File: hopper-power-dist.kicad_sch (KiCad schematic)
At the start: 23 parts

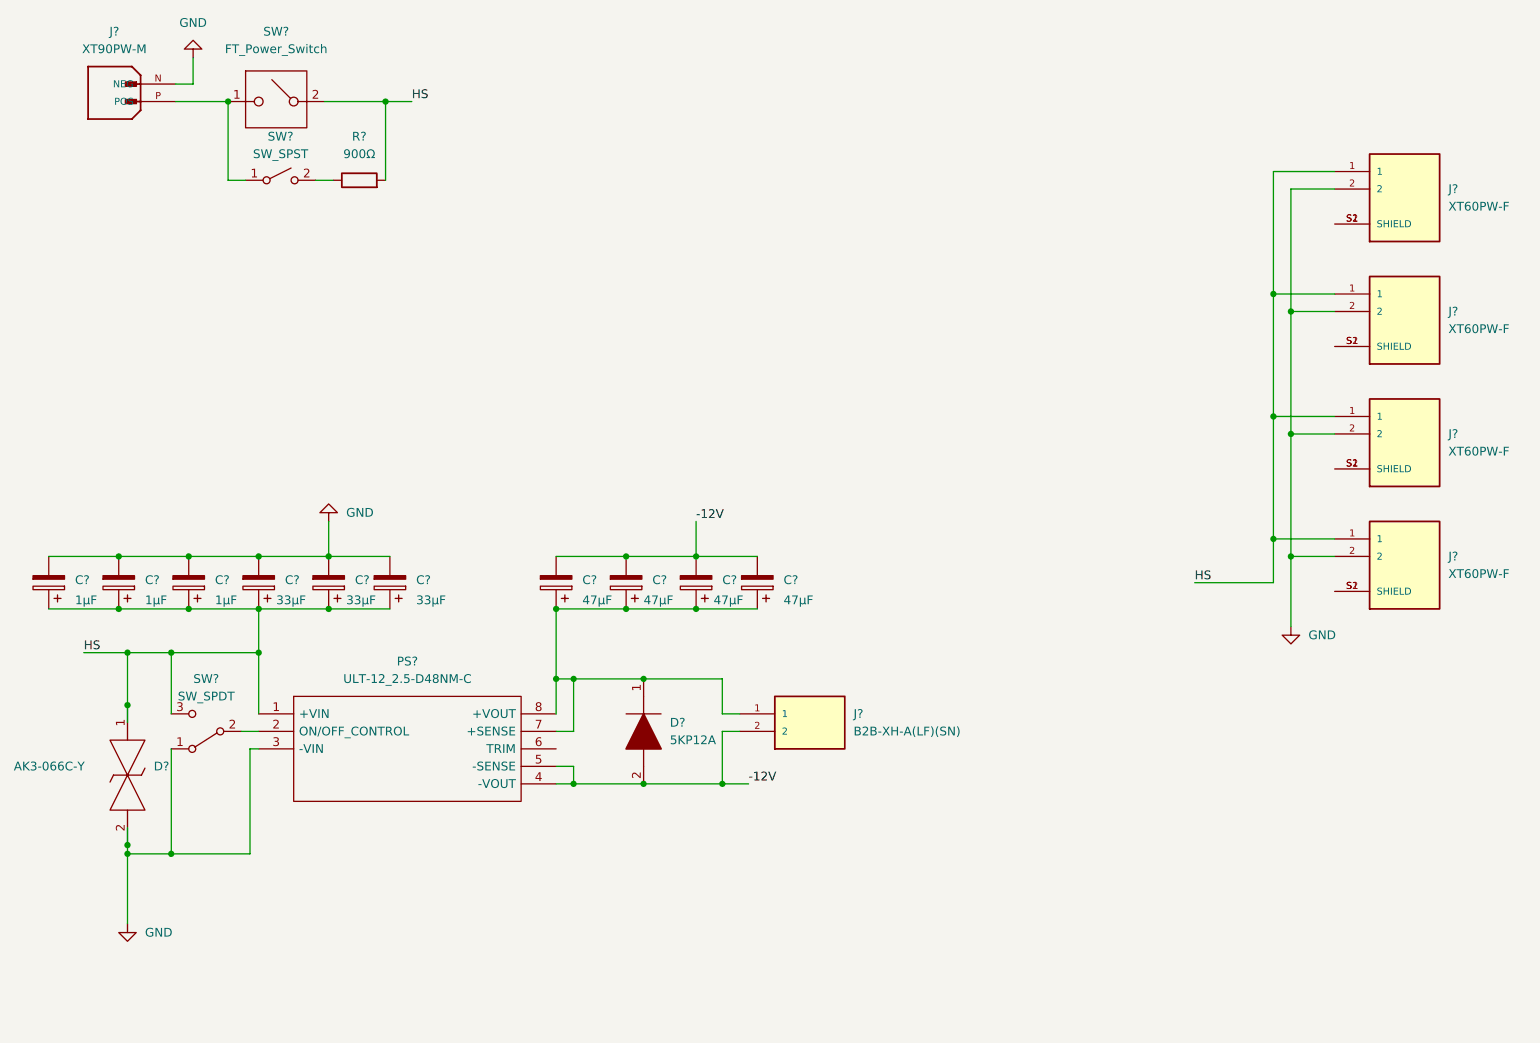
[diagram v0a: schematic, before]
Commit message: Initialize PCB, update gitignore
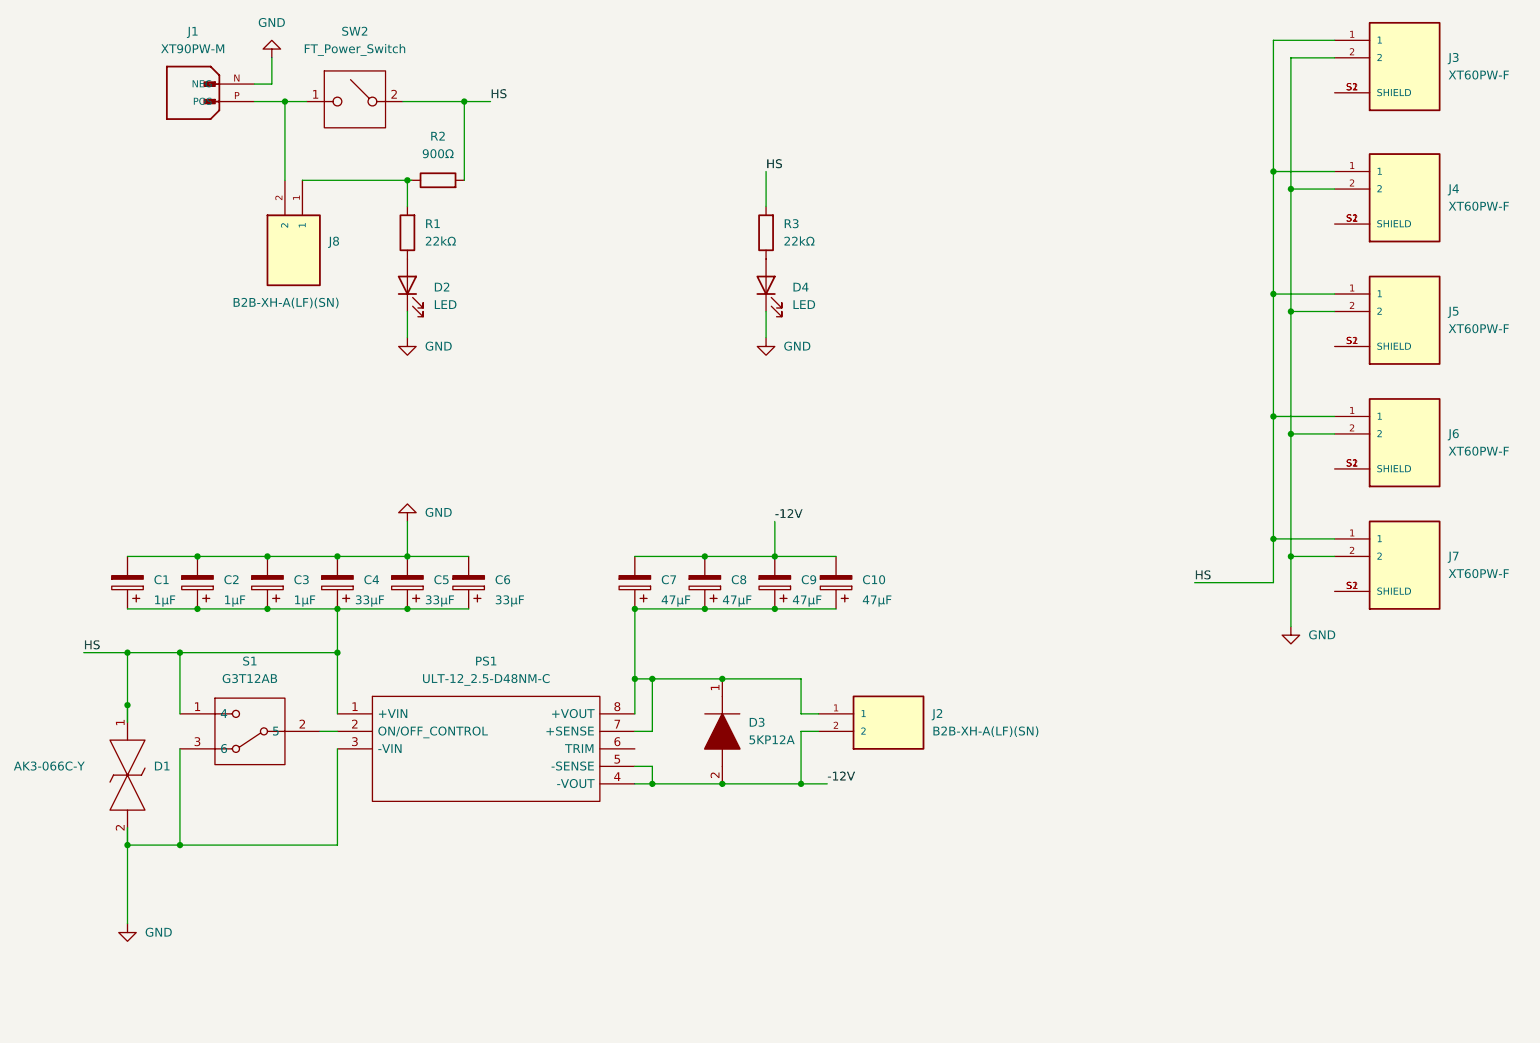
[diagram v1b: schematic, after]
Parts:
- removed SW?: SW_SPDT, symbol Switch:SW_SPDT
- removed SW?: SW_SPST, symbol Switch:SW_SPST
- added D2, D4: LED, LED_SMD:LED_0603_1608Metric, symbol Device:LED
- added J3: XT60PW-F, XT60PW-F:AMASS_XT60PW-F, symbol XT60PW-F:XT60PW-F
- added J8: B2B-XH-A(LF)(SN), B2B-XH-A_LF__SN_:JST_B2B-XH-A(LF)(SN), symbol B2B-XH-A_LF__SN_:B2B-XH-A(LF)(SN)
- added R1, R3: 22kΩ, Resistor_SMD:R_0603_1608Metric_Pad0.98x0.95mm_HandSolder, symbol Device:R
- added S1: G3T12AB, G3T12AB, symbol SamacSys_Parts:G3T12AB
- C1, C10, C2, C3, C4, C5, C6, C7, C8, C9: renamed from C?; footprint (none) -> Capacitor_SMD:CP_Elec_8x10
- D1: renamed from D?; footprint AK3066CY -> SamacSys_Parts:AK3066CY
- D3: renamed from D?; footprint DIOAD4425W136L885D885 -> SamacSys_Parts:DIOAD4425W136L885D885
- J1: renamed from J?; footprint AMASS_XT90PW-M -> XT90PW-M:AMASS_XT90PW-M
- J2: renamed from J?; footprint JST_B2B-XH-A(LF)(SN) -> B2B-XH-A_LF__SN_:JST_B2B-XH-A(LF)(SN)
- J4, J5, J6, J7: renamed from J?; footprint AMASS_XT60PW-F -> XT60PW-F:AMASS_XT60PW-F
- PS1: renamed from PS?; footprint ULT1225D48NMC -> SamacSys_Parts:ULT1225D48NMC
- R2: renamed from R?; footprint (none) -> SamacSys_Parts:RESAD5390W86L2222D792
- gave numbers to parts that had none: 1
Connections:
- net GND: now also D2.1 (K), D4.1 (K), J3.2, S1.3 (6)
- net HS: now also J3.1, R3.2, S1.1 (4)
- net at J1.P (POS), SW2.1: now also J8.2
- net at PS1.2 (ON/OFF_CONTROL): now also S1.2 (5)
- net at R2.1: now also J8.1, R1.2
- new net: D4.2 (A), R3.1
- new net: D2.2 (A), R1.1
- new net: J3.S1 (SHIELD), J3.S2 (SHIELD)
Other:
- moved on the sheet: C1, C10, C2, C3, C4, C5, C6, C7, C8, C9, D3, J1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

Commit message: Create basic PCB layout
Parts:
- added D5: LED, LED_SMD:LED_0603_1608Metric, symbol Device:LED
- added R4: 22kΩ, Resistor_SMD:R_0603_1608Metric_Pad0.98x0.95mm_HandSolder, symbol Device:R
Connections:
- net GND: now also J3.S1 (SHIELD), J3.S2 (SHIELD), J4.S1 (SHIELD), J4.S2 (SHIELD), J5.S1 (SHIELD), J5.S2 (SHIELD), J6.S1 (SHIELD), J6.S2 (SHIELD), J7.S1 (SHIELD), J7.S2 (SHIELD), D5.1 (K)
- net at PS1.2 (ON/OFF_CONTROL), S1.2 (5): now also R4.2
- new net: D5.2 (A), R4.1
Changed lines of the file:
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@@
   (junction (at 208.28 93.98) (diameter 0) (color 0 0 0 0)
   )
+  (junction (at 214.63 58.42) (diameter 0) (color 0 0 0 0)
+  )
   (junction (at 39.37 133.35) (diameter 0) (color 0 0 0 0)
   )
@@
   (junction (at 205.74 91.44) (diameter 0) (color 0 0 0 0)
   )
+  (junction (at 214.63 39.37) (diameter 0) (color 0 0 0 0)
+  )
   (junction (at 39.37 125.73) (diameter 0) (color 0 0 0 0)
   )
   (junction (at 113.03 129.54) (diameter 0) (color 0 0 0 0)
   )
+  (junction (at 214.63 76.2) (diameter 0) (color 0 0 0 0)
+  )
   (junction (at 208.28 111.76) (diameter 0) (color 0 0 0 0)
   )
+  (junction (at 67.31 137.16) (diameter 0) (color 0 0 0 0)
+  )
   (junction (at 115.57 144.78) (diameter 0) (color 0 0 0 0)
   )
@@
   (junction (at 205.74 109.22) (diameter 0) (color 0 0 0 0)
   )
+  (junction (at 214.63 93.98) (diameter 0) (color 0 0 0 0)
+  )
   (junction (at 133.35 119.38) (diameter 0) (color 0 0 0 0)
   )
@@
   (junction (at 115.57 129.54) (diameter 0) (color 0 0 0 0)
   )
+  (junction (at 214.63 111.76) (diameter 0) (color 0 0 0 0)
+  )
   (junction (at 88.265 45.72) (diameter 0) (color 0 0 0 0)
   )
@@
     (stroke (width 0) (type default) (color 0 0 0 0))
   )
+  (wire (pts (xy 214.63 58.42) (xy 214.63 63.5))
+    (stroke (width 0) (type default) (color 0 0 0 0))
+  )
   (wire (pts (xy 115.57 129.54) (xy 125.73 129.54))
     (stroke (width 0) (type default) (color 0 0 0 0))
@@
     (stroke (width 0) (type default) (color 0 0 0 0))
   )
+  (wire (pts (xy 214.63 39.37) (xy 214.63 44.45))
+    (stroke (width 0) (type default) (color 0 0 0 0))
+  )
+  (wire (pts (xy 63.5 173.99) (xy 63.5 177.8))
+    (stroke (width 0) (type default) (color 0 0 0 0))
+  )
   (wire (pts (xy 49.53 111.76) (xy 59.69 111.76))
     (stroke (width 0) (type default) (color 0 0 0 0))
@@
     (stroke (width 0) (type default) (color 0 0 0 0))
   )
+  (wire (pts (xy 63.5 158.75) (xy 63.5 147.32))
+    (stroke (width 0) (type default) (color 0 0 0 0))
+  )
   (wire (pts (xy 46.99 125.73) (xy 46.99 134.62))
     (stroke (width 0) (type default) (color 0 0 0 0))
@@
     (stroke (width 0) (type default) (color 0 0 0 0))
   )
+  (wire (pts (xy 214.63 111.76) (xy 214.63 116.84))
+    (stroke (width 0) (type default) (color 0 0 0 0))
+  )
   (wire (pts (xy 208.28 111.76) (xy 214.63 111.76))
     (stroke (width 0) (type default) (color 0 0 0 0))
@@
     (stroke (width 0) (type default) (color 0 0 0 0))
   )
+  (wire (pts (xy 67.31 137.16) (xy 67.31 147.32))
+    (stroke (width 0) (type default) (color 0 0 0 0))
+  )
   (wire (pts (xy 113.03 111.76) (xy 123.19 111.76))
     (stroke (width 0) (type default) (color 0 0 0 0))
@@
     (stroke (width 0) (type default) (color 0 0 0 0))
   )
+  (wire (pts (xy 214.63 93.98) (xy 214.63 99.06))
+    (stroke (width 0) (type default) (color 0 0 0 0))
+  )
   (wire (pts (xy 69.85 139.7) (xy 69.85 153.67))
     (stroke (width 0) (type default) (color 0 0 0 0))
@@
     (stroke (width 0) (type default) (color 0 0 0 0))
   )
+  (wire (pts (xy 214.63 76.2) (xy 214.63 81.28))
+    (stroke (width 0) (type default) (color 0 0 0 0))
+  )
   (wire (pts (xy 113.03 119.38) (xy 123.19 119.38))
     (stroke (width 0) (type default) (color 0 0 0 0))
@@
   )
   (wire (pts (xy 205.74 91.44) (xy 205.74 109.22))
+    (stroke (width 0) (type default) (color 0 0 0 0))
+  )
+  (wire (pts (xy 63.5 147.32) (xy 67.31 147.32))
     (stroke (width 0) (type default) (color 0 0 0 0))
   )
@@
   (label "HS" (at 92.075 45.72 0)
     (effects (font (size 1.27 1.27)) (justify left bottom))
+  )
+  (symbol (lib_id "Device:R") (at 63.5 162.56 180) (unit 1)
+    (in_bom yes) (on_board yes)
+    (property "Reference" "R4" (id 0) (at 66.04 161.2899 0)
+      (effects (font (size 1.27 1.27)) (justify right))
+    )
+    (property "Value" "22kΩ" (id 1) (at 66.04 163.8299 0)
+      (effects (font (size 1.27 1.27)) (justify right))
+    )
+    (property "Footprint" "Resistor_SMD:R_0603_1608Metric_Pad0.98x0.95mm_HandSolder" (id 2) (at 65.278 162.56 90)
+      (effects (font (size 1.27 1.27)) hide)
+    )
+    (property "Datasheet" "~" (id 3) (at 63.5 162.56 0)
+      (effects (font (size 1.27 1.27)) hide)
+    )
+    (pin "1")
+    (pin "2")
   )
   (symbol (lib_id "Device:C_Polarized") (at 88.9 115.57 180) (unit 1)
@@
     (pin "2")
   )
+  (symbol (lib_id "Device:LED") (at 63.5 170.18 90) (unit 1)
+    (in_bom yes) (on_board yes) (fields_autoplaced)
+    (property "Reference" "D5" (id 0) (at 67.31 170.4974 90)
+      (effects (font (size 1.27 1.27)) (justify right))
+    )
+    (property "Value" "LED" (id 1) (at 67.31 173.0374 90)
+      (effects (font (size 1.27 1.27)) (justify right))
+    )
+    (property "Footprint" "LED_SMD:LED_0603_1608Metric" (id 2) (at 63.5 170.18 0)
+      (effects (font (size 1.27 1.27)) hide)
+    )
+    (property "Datasheet" "~" (id 3) (at 63.5 170.18 0)
+      (effects (font (size 1.27 1.27)) hide)
+    )
+    (pin "1")
+    (pin "2")
+  )
   (symbol (lib_id "SamacSys_Parts:G3T12AB") (at 46.99 134.62 0) (unit 1)
     (in_bom yes) (on_board yes) (fields_autoplaced)
@@
     (pin "1")
     (pin "2")
+  )
+  (symbol (lib_id "power:GND") (at 63.5 177.8 0) (unit 1)
+    (in_bom yes) (on_board yes) (fields_autoplaced)
+    (property "Reference" "#PWR07" (id 0) (at 63.5 184.15 0)
+      (effects (font (size 1.27 1.27)) hide)
+    )
+    (property "Value" "GND" (id 1) (at 66.04 179.0699 0)
+      (effects (font (size 1.27 1.27)) (justify left))
+    )
+    (property "Footprint" "" (id 2) (at 63.5 177.8 0)
+      (effects (font (size 1.27 1.27)) hide)
+    )
+    (property "Datasheet" "" (id 3) (at 63.5 177.8 0)
+      (effects (font (size 1.27 1.27)) hide)
+    )
+    (pin "1")
   )
   (symbol (lib_id "Device:R") (at 84.455 57.15 90) (unit 1)
@@
       (reference "#PWR06") (unit 1) (value "GND") (footprint "")
     )
+    (path "/bfd44d27-a5fa-4043-8089-d8d133b26157"
+      (reference "#PWR07") (unit 1) (value "GND") (footprint "")
+    )
     (path "/f00aaf0e-6472-4dd6-aa6d-05ba502461cd"
       (reference "C1") (unit 1) (value "1μF") (footprint "Capacitor_SMD:CP_Elec_8x10")
@@
       (reference "D4") (unit 1) (value "LED") (footprint "LED_SMD:LED_0603_1608Metric")
     )
+    (path "/844b6202-1707-4575-915c-796522b05ffe"
+      (reference "D5") (unit 1) (value "LED") (footprint "LED_SMD:LED_0603_1608Metric")
+    )
     (path "/f9327447-8d91-4143-800f-2749f41e196a"
       (reference "J1") (unit 1) (value "XT90PW-M") (footprint "XT90PW-M:AMASS_XT90PW-M")
@@
       (reference "R3") (unit 1) (value "22kΩ") (footprint "Resistor_SMD:R_0603_1608Metric_Pad0.98x0.95mm_HandSolder")
     )
+    (path "/051432d1-ff3d-44c0-aa33-f2f8ef30a5ff"
+      (reference "R4") (unit 1) (value "22kΩ") (footprint "Resistor_SMD:R_0603_1608Metric_Pad0.98x0.95mm_HandSolder")
+    )
     (path "/934c6aeb-1840-4de5-bdba-64e972c9f98d"
